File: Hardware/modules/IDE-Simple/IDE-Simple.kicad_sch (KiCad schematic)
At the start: 9 parts, among them J1 Conn_02x20_Odd_Even, J2 Conn_02x22_Odd_Even, J3 Bus_PCI_6502, U1 74HC138, U2 74AHC2G00

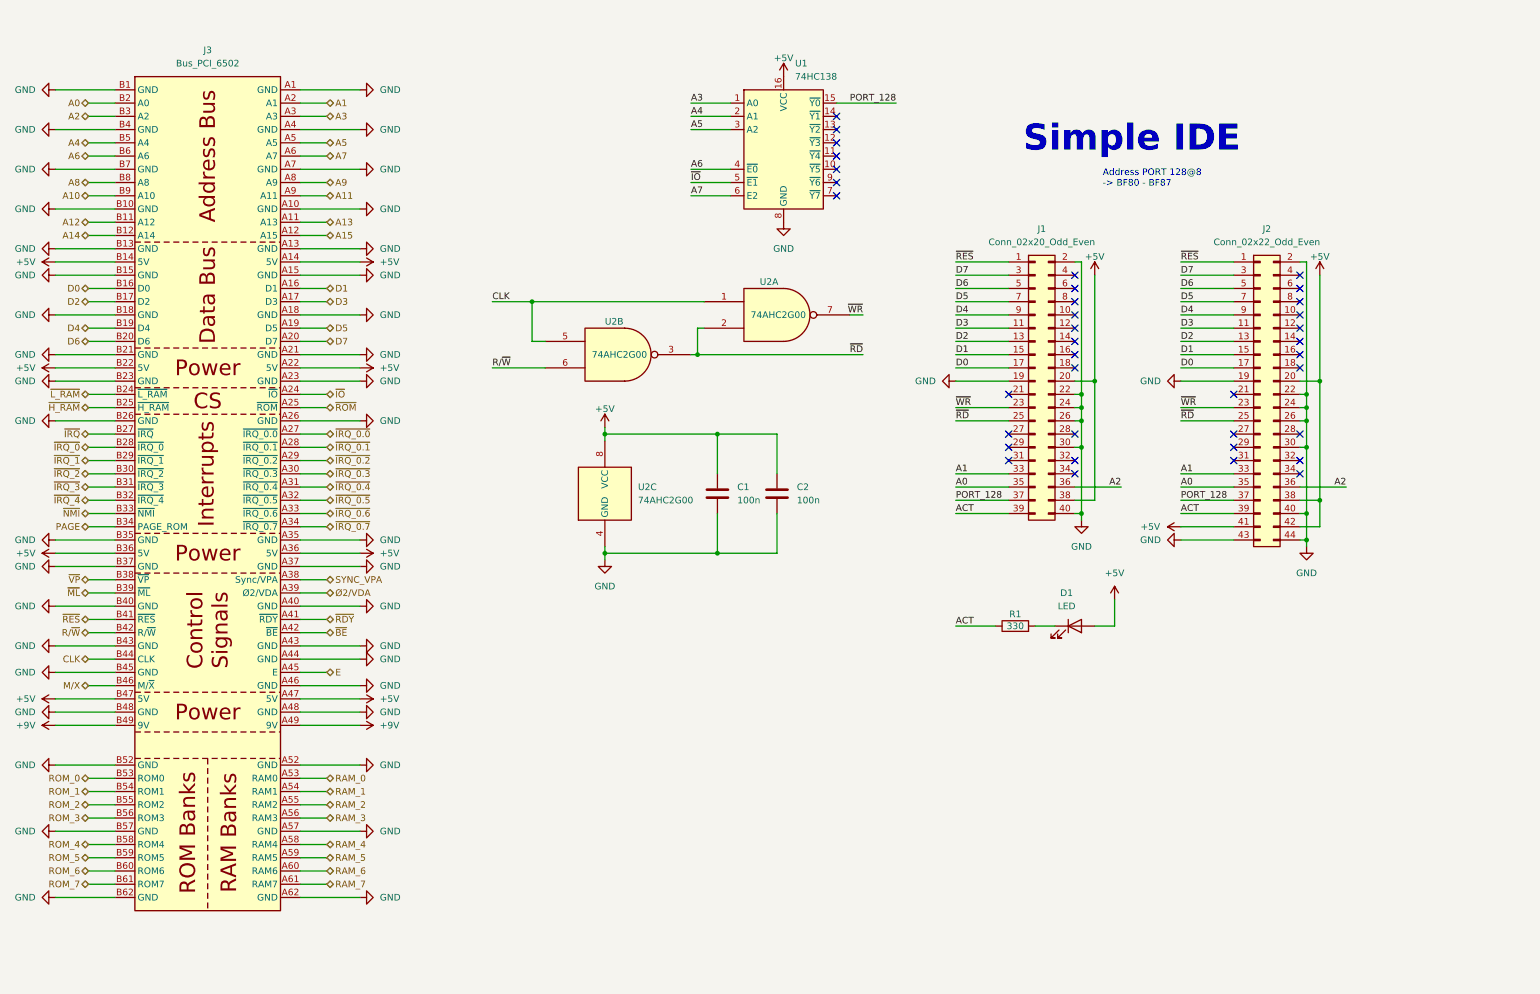
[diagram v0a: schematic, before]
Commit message: Hardware Update Add MyCPU VGA Module Beautify all Schematics minor Error corrections Readme Update
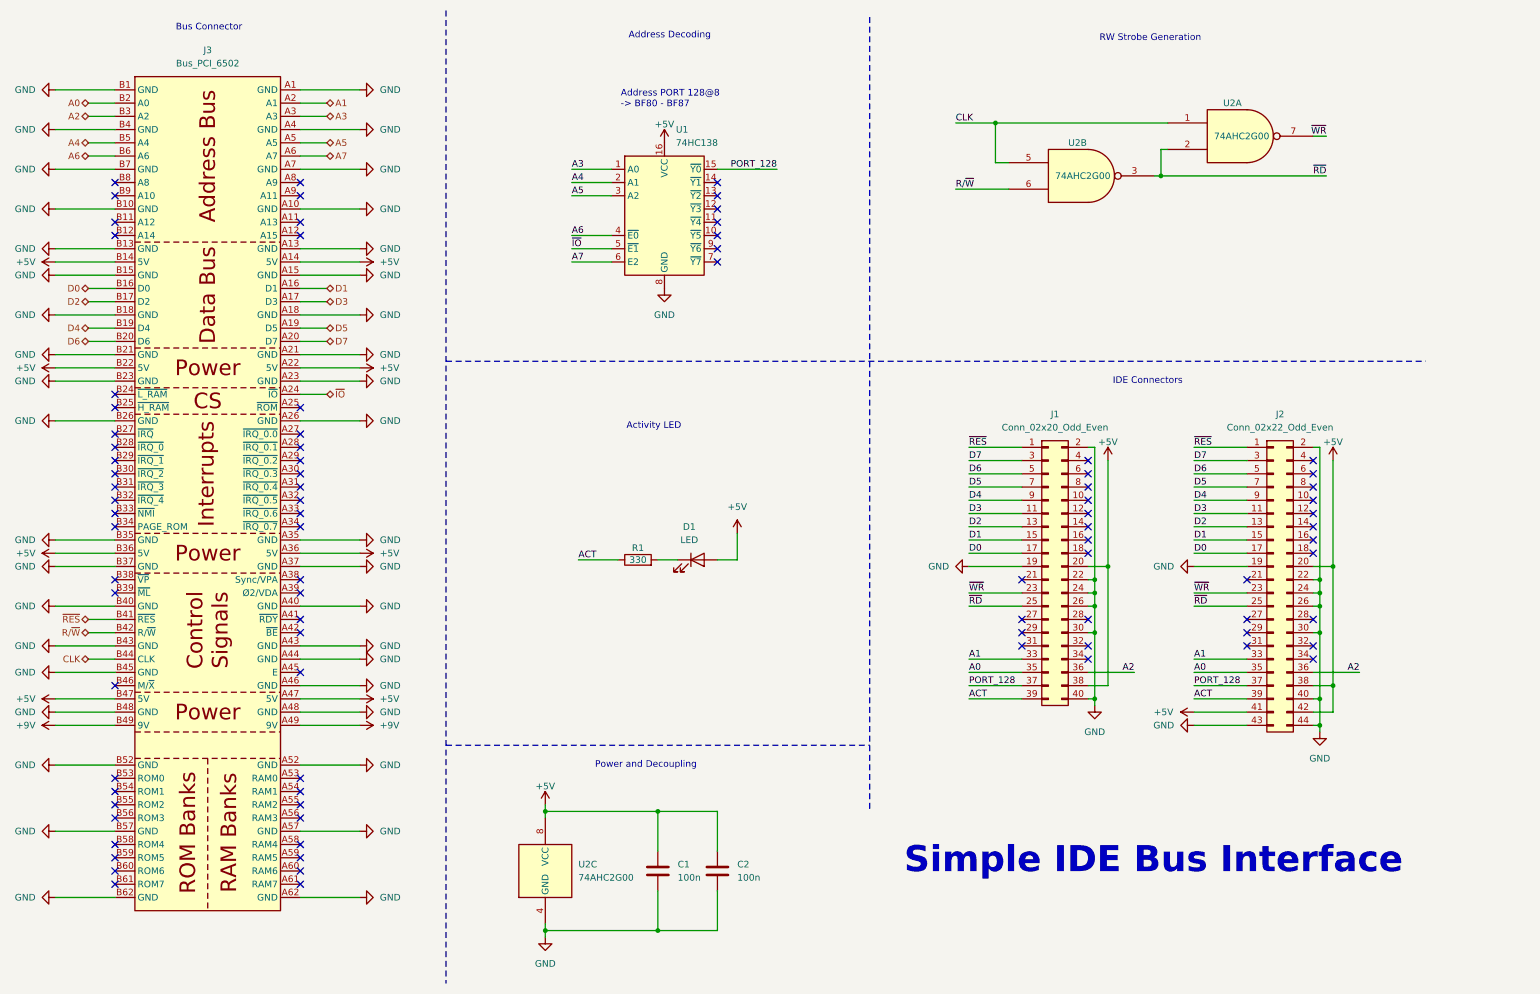
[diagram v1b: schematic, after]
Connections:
- net A10: no longer names the net of J3.B9 (A10)
- net A11: no longer names the net of J3.A9 (A11)
- net A12: no longer names the net of J3.B11 (A12)
- net A13: no longer names the net of J3.A11 (A13)
- net A14: no longer names the net of J3.B12 (A14)
- net A15: no longer names the net of J3.A12 (A15)
- net A8: no longer names the net of J3.B8 (A8)
- net A9: no longer names the net of J3.A8 (A9)
- net E: no longer names the net of J3.A45 (E)
- net M/X: no longer names the net of J3.B46 (M/~{X})
- net PAGE: no longer names the net of J3.B34 (PAGE_ROM)
- net RAM_0: no longer names the net of J3.A53 (RAM0)
- net RAM_1: no longer names the net of J3.A54 (RAM1)
- net RAM_2: no longer names the net of J3.A55 (RAM2)
- net RAM_3: no longer names the net of J3.A56 (RAM3)
- net RAM_4: no longer names the net of J3.A58 (RAM4)
- net RAM_5: no longer names the net of J3.A59 (RAM5)
- net RAM_6: no longer names the net of J3.A60 (RAM6)
- net RAM_7: no longer names the net of J3.A61 (RAM7)
- net ROM_0: no longer names the net of J3.B53 (ROM0)
- net ROM_1: no longer names the net of J3.B54 (ROM1)
- net ROM_2: no longer names the net of J3.B55 (ROM2)
- net ROM_3: no longer names the net of J3.B56 (ROM3)
- net ROM_4: no longer names the net of J3.B58 (ROM4)
- net ROM_5: no longer names the net of J3.B59 (ROM5)
- net ROM_6: no longer names the net of J3.B60 (ROM6)
- net ROM_7: no longer names the net of J3.B61 (ROM7)
- net SYNC_VPA: no longer names the net of J3.A38 (Sync/VPA)
- net ~{BE}: no longer names the net of J3.A42 (~{BE})
- net ~{H_RAM}: no longer names the net of J3.B25 (~{H_RAM})
- net ~{IRQ_0.0}: no longer names the net of J3.A27 (~{IRQ_0.0})
- net ~{IRQ_0.1}: no longer names the net of J3.A28 (~{IRQ_0.1})
- net ~{IRQ_0.2}: no longer names the net of J3.A29 (~{IRQ_0.2})
- net ~{IRQ_0.3}: no longer names the net of J3.A30 (~{IRQ_0.3})
- net ~{IRQ_0.4}: no longer names the net of J3.A31 (~{IRQ_0.4})
- net ~{IRQ_0.5}: no longer names the net of J3.A32 (~{IRQ_0.5})
- net ~{IRQ_0.6}: no longer names the net of J3.A33 (~{IRQ_0.6})
- net ~{IRQ_0.7}: no longer names the net of J3.A34 (~{IRQ_0.7})
- net ~{IRQ_0}: no longer names the net of J3.B28 (~{IRQ_0})
- net ~{IRQ_1}: no longer names the net of J3.B29 (~{IRQ_1})
- net ~{IRQ_2}: no longer names the net of J3.B30 (~{IRQ_2})
- net ~{IRQ_3}: no longer names the net of J3.B31 (~{IRQ_3})
- net ~{IRQ_4}: no longer names the net of J3.B32 (~{IRQ_4})
- net ~{IRQ}: no longer names the net of J3.B27 (~{IRQ})
- net ~{L_RAM}: no longer names the net of J3.B24 (~{L_RAM})
- net ~{ML}: no longer names the net of J3.B39 (~{ML})
- net ~{NMI}: no longer names the net of J3.B33 (~{NMI})
- net ~{RDY}: no longer names the net of J3.A41 (~{RDY})
- net ~{ROM}: no longer names the net of J3.A25 (~{ROM})
- net ~{VP}: no longer names the net of J3.B38 (~{VP})
- net Ø2/VDA: no longer names the net of J3.A39 (Ø2/VDA)
- no-connect marks 37 -> 88
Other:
- note added: "Activity LED"
- note added: "Address Decoding"
- note added: "Bus Connector"
- note added: "IDE Connectors"
- note added: "Power and Decoupling"
- note added: "RW Strobe Generation"
- note added: "Simple IDE Bus Interface"
- note removed: "Simple IDE"
- company: (none) -> Synthron
- title: (none) -> S65xx Computer System
- moved on the sheet: C1, C2, D1, J1, J2, R1, U1, U2A, U2B, U2C
